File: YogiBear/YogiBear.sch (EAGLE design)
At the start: 19 parts, among them IC1 VNH2SP30, Q1 P-CHANNEL-MOSFETTO252

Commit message: Finish Yogi Bear and approved by Seiya
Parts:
- removed C2: 470 uF, pie:CAP_POLG
- added DIAGA, MOTA: RED, pie:LED0603
- added DIAGB, MOTB: YELLOW, pie:LED0603
- added R12, R13, R14, R15: 330, pie:R-US_R0603
- Q1: value P-CHANNEL-MOSFETTO252 -> N-CHANNEL-MOSFETTO252; device pie:P-CHANNEL-MOSFETTO252 -> pie:N-CHANNEL-MOSFETTO252
- R1, R2: value 3.3K -> 4.7K; device adafruit:R-US_R0603 -> pie:R-US_R0603
- R10, R11, R3, R4, R5, R6, R7, R9: device adafruit:R-US_R0603 -> pie:R-US_R0603
- R8: value (none) -> 10K; device adafruit:R-US_R0603 -> pie:R-US_R0603
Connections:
- removed net VIN: C2.+, IC1.NC5, IC1.NC6, IC1.NC7, IC1.NC8, R11.2, VBAT.VCC
- new net 12V: IC1.NC5, IC1.NC6, IC1.NC7, IC1.NC8, IC1.VCC, IC1.VCC@1, IC1.VCC@2, IC1.VCC@3, IC1.VCC@4, R11.2, VBAT.VCC
- new net BATGND: Q1.S@2, VBAT.GND
- new net LED1: DIAGA.A, U$1.A3
- new net LED2: DIAGB.A, U$1.A2
- new net LED3: MOTA.A, U$1.A1
- new net LED4: MOTB.A, U$1.A0
- new net N$10: DIAGA.C, R12.1
- new net N$7: MOTB.C, R15.1
- new net N$8: MOTA.C, R14.1
- new net N$9: DIAGB.C, R13.1
- net GND: now also R12.2, R13.2, R14.2, R15.2; no longer C2.-, Q1.S, VBAT.GND
- net VCC: now also U$1.VCC; no longer IC1.VCC, IC1.VCC@1, IC1.VCC@2, IC1.VCC@3, IC1.VCC@4
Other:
- moved on the sheet: R11

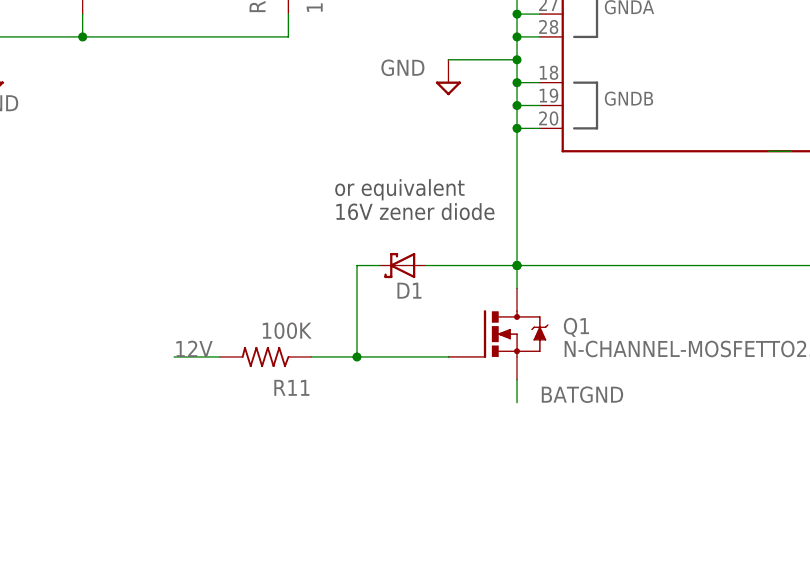
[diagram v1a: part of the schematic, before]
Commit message: Replaced reverse polarity diode  with PiE library generic diode package
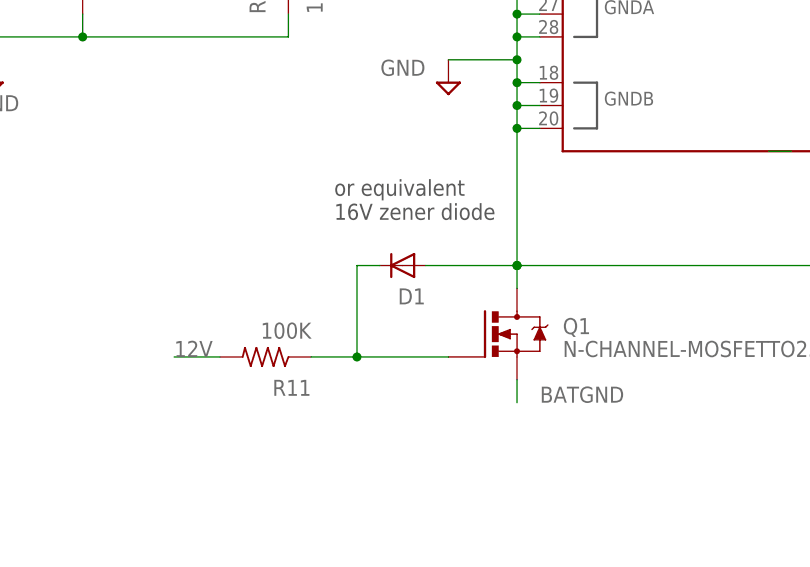
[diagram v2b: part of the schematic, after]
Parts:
- D1: device diode:SCHOTTKY-DIODESMC -> pie:DIODESMA-ALT
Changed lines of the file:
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@@
 <?xml version="1.0" encoding="utf-8"?>
 <!DOCTYPE eagle SYSTEM "eagle.dtd">
-<eagle version="7.6.0">
+<eagle version="7.3.0">
 <drawing>
 <settings>
@@
 <part name="C1" library="pie" deviceset="CAP" device="0603-CAP" value="33 nF"/>
 <part name="P+4" library="supply1" deviceset="VCC" device=""/>
-<part name="D1" library="diode" deviceset="SCHOTTKY-DIODE" device="SMC"/>
+<part name="D1" library="pie" deviceset="DIODE" device="SMA-ALT"/>
 <part name="FRAME1" library="pie" deviceset="FRAME-LETTER" device=""/>
 <part name="U$1" library="pie" deviceset="ARDUINO_PRO_MICRO" device=""/>
